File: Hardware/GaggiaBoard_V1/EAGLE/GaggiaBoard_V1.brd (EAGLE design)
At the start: 80 x 100 mm, 64 parts, among them IC1 LD117ADT33TR, J2 Vertical Qwiic Connector, J3 Vertical Qwiic Connector, J4 1X2-3.5MM, J5 1X2-3.5MM, K1 RELAY-SPDT-JZC-11F, K2 RELAY-SPDT-JZC-11F, K3 RELAY-SPDT-JZC-11F, Q1 600mA/40V, Q2 600mA/40V, Q3 600mA/40V, Q4 600mA/40V, Q5 600mA/40V, Q6 600mA/40V, U1 BLACKPILL, U2 MAX31855K, U3 MAX31855K, U4 MOC3021MDIL06O

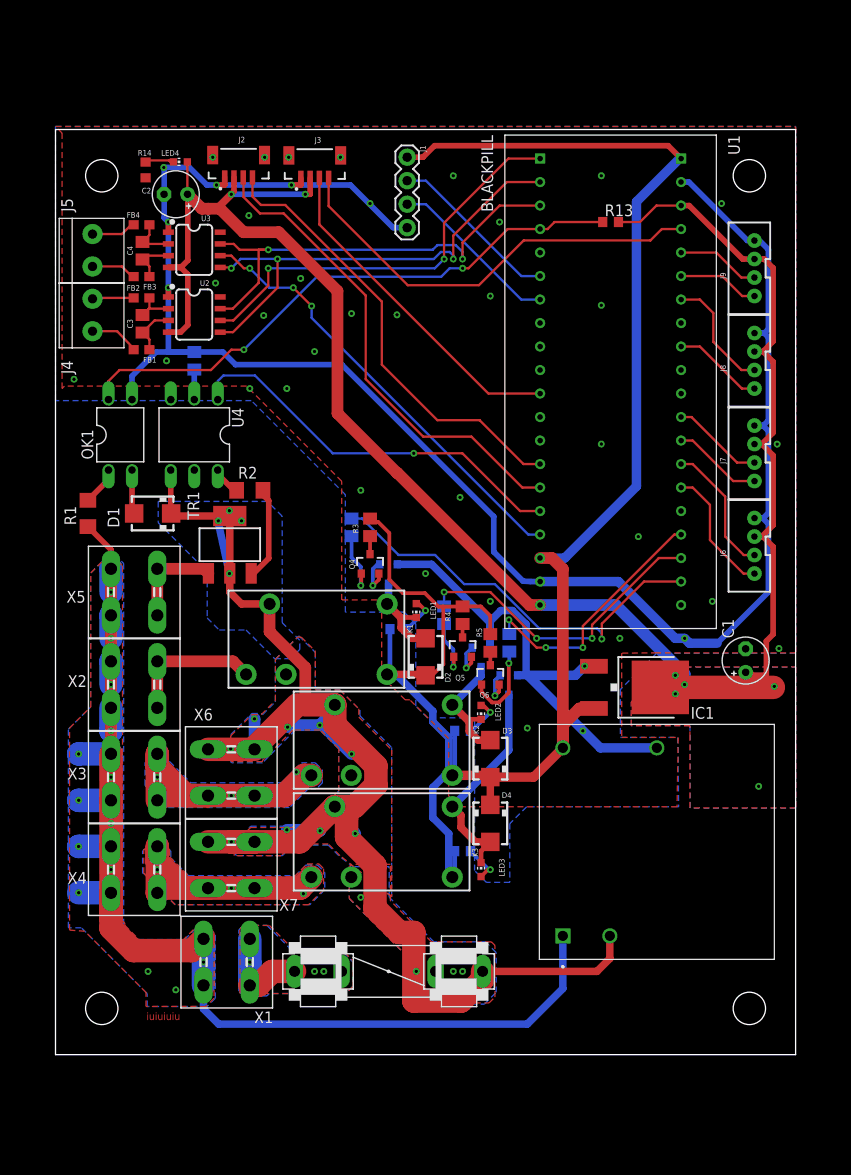
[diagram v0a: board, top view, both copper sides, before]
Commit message: Fiducials added
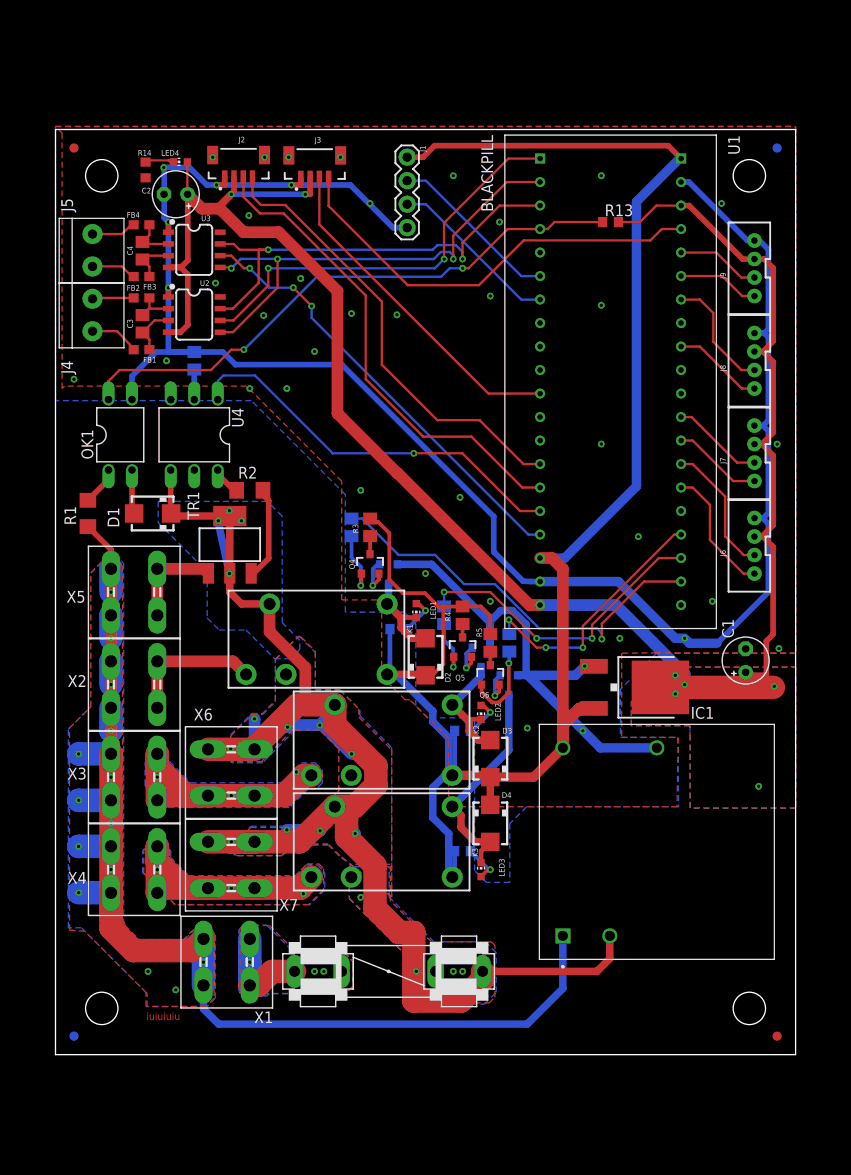
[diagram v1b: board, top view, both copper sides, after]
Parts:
- added MARK1, MARK2, MARK3, MARK4: FIDUCIAL, adafruit:FIDUCIAL_1MM
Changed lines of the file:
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@@
 <setting verticaltext="up"/>
 </settings>
-<grid distance="50" unitdist="mil" unit="mil" style="lines" multiple="1" display="no" altdistance="5" altunitdist="mil" altunit="mil"/>
+<grid distance="1" unitdist="mm" unit="mm" style="lines" multiple="1" display="no" altdistance="0.1" altunitdist="mm" altunit="mm"/>
 <layers>
 <layer number="1" name="Top" color="4" fill="1" visible="yes" active="yes"/>
@@
 <attribute name="VALUE" x="11.643" y="94.992" size="1.27" layer="27" rot="R90"/>
 </element>
+<element name="MARK2" library="adafruit" library_urn="urn:adsk.eagle:library:420" package="FIDUCIAL_1MM" package3d_urn="urn:adsk.eagle:package:6240632/1" value="FIDUCIAL" x="2" y="2" smashed="yes" rot="MR0"/>
+<element name="MARK4" library="adafruit" library_urn="urn:adsk.eagle:library:420" package="FIDUCIAL_1MM" package3d_urn="urn:adsk.eagle:package:6240632/1" value="FIDUCIAL" x="78" y="98" smashed="yes" rot="MR0"/>
+<element name="MARK3" library="adafruit" library_urn="urn:adsk.eagle:library:420" package="FIDUCIAL_1MM" package3d_urn="urn:adsk.eagle:package:6240632/1" value="FIDUCIAL" x="78" y="2" smashed="yes"/>
+<element name="MARK1" library="adafruit" library_urn="urn:adsk.eagle:library:420" package="FIDUCIAL_1MM" package3d_urn="urn:adsk.eagle:package:6240632/1" value="FIDUCIAL" x="2" y="98" smashed="yes"/>
 </elements>
 <signals>

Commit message: UART level shifter
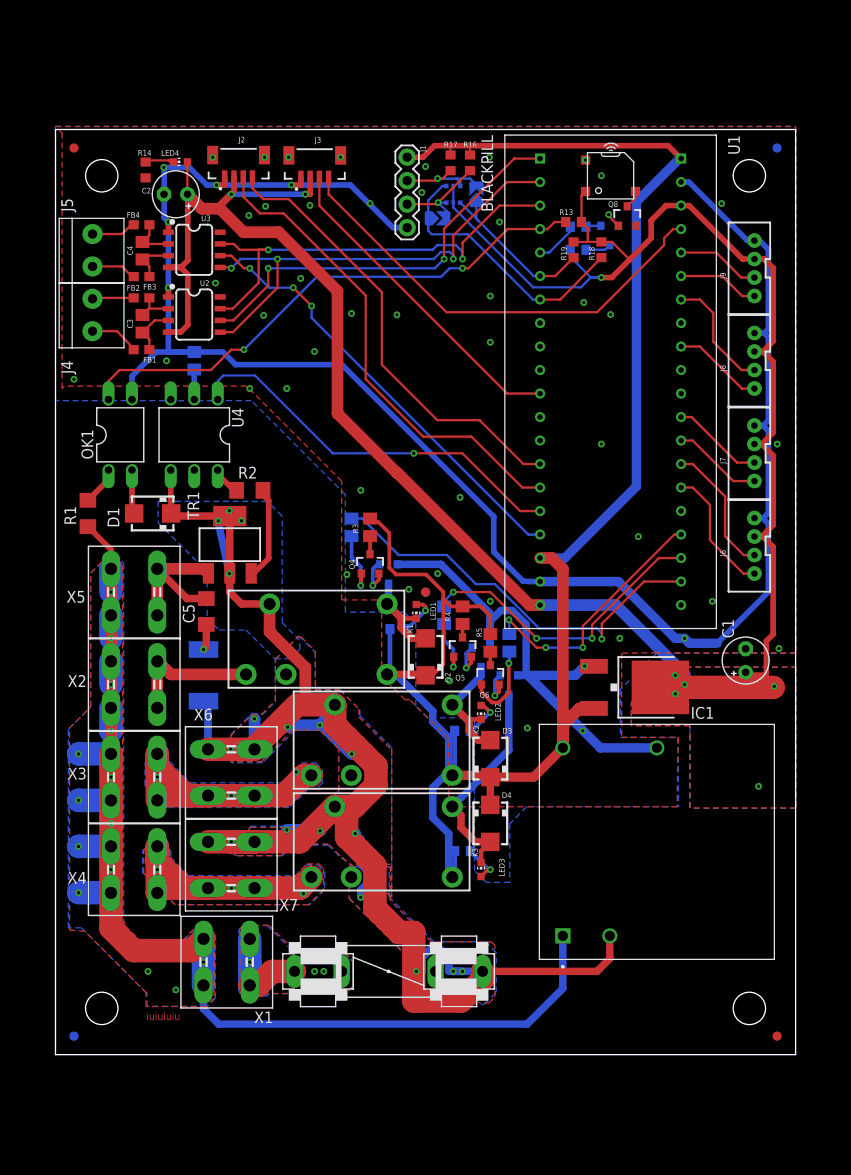
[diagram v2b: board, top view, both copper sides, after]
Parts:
- added C5: 10nF, rcl:C1206
- added MARK5, MARK6: FIDUCIAL, adafruit:FIDUCIAL_1MM
- added Q7: (no value), microbuilder:SOT363
- added Q8, Q9: 600mA/40V, SparkFun-DiscreteSemi:SOT23-3
- added R15: 220, rcl:R2512
- added R16, R17, R18, R19, R20, R21: 10K, rcl:R0603
- added SJ1, SJ2: (no value), microbuilder:SOLDERJUMPER_ARROW_NOPASTE
- added SPK1: SMT-0540-S-R, adafruit:SMT-0540-S-R
- moved R13 4.00 mm to (56.0, 90.0)
- moved LED1 0.10 mm to (39.0, 47.9)
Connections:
- new net N$30: Q8.3, SPK1.-
- new net N$32: C5.1, R15.2
- new net N$33: Q8.1, Q9.2
- new net N$34: Q9.1, R20.2
- new net N$35: Q9.3, R21.1
- new net PA8: R20.1, U1.P1$5
- new net UART1_5V_RX: J1.3, Q7.3, R16.1, SJ2.2
- new net UART1_5V_TX: J1.2, Q7.6, R17.1, SJ1.2
- net 3V3: now also Q7.2, Q7.5, R18.2, R19.2, R21.2, SPK1.+
- net 5V: now also R16.2, R17.2
- net AC_P: now also R15.1
- net GND: now also Q8.2
- net PUMP_P: now also C5.2
- net UART1_RX: now also Q7.4, R18.1, SJ2.1; no longer J1.3
- net UART1_TX: now also Q7.1, R19.1, SJ1.1; no longer J1.2
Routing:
- net 3V3: track 215.8 -> 257.8 mm, vias 7 -> 8
- net AC_P: track 179.6 -> 204.6 mm
- net UART1_5V_RX: track 0.00 -> 11.3 mm, vias 0 -> 1
- net UART1_RX: track 18.6 -> 29.6 mm
- net UART1_5V_TX: track 0.00 -> 10.6 mm, vias 0 -> 1
- net PUMP_P: track 10.8 -> 17.4 mm
- net AC_N: track 148.0 -> 141.9 mm
- net PA8: track 0.00 -> 4.73 mm
- net PB15: track 62.5 -> 58.5 mm
- net N$33: track 0.00 -> 3.27 mm, vias 0 -> 1
- net N$32: track 0.00 -> 2.82 mm, vias 0 -> 1
- net N$35: track 0.00 -> 2.76 mm
- net 5V: track 202.8 -> 205.4 mm
- net I2C2_SCL: track 47.2 -> 49.3 mm
- net N$30: track 0.00 -> 1.97 mm
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
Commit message: GaggiaBoard BOM update
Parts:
- Q7: value (none) -> 2N7002D
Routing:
- net GND: track 259.1 -> 260.3 mm
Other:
- outline, holes or cut-outs redrawn

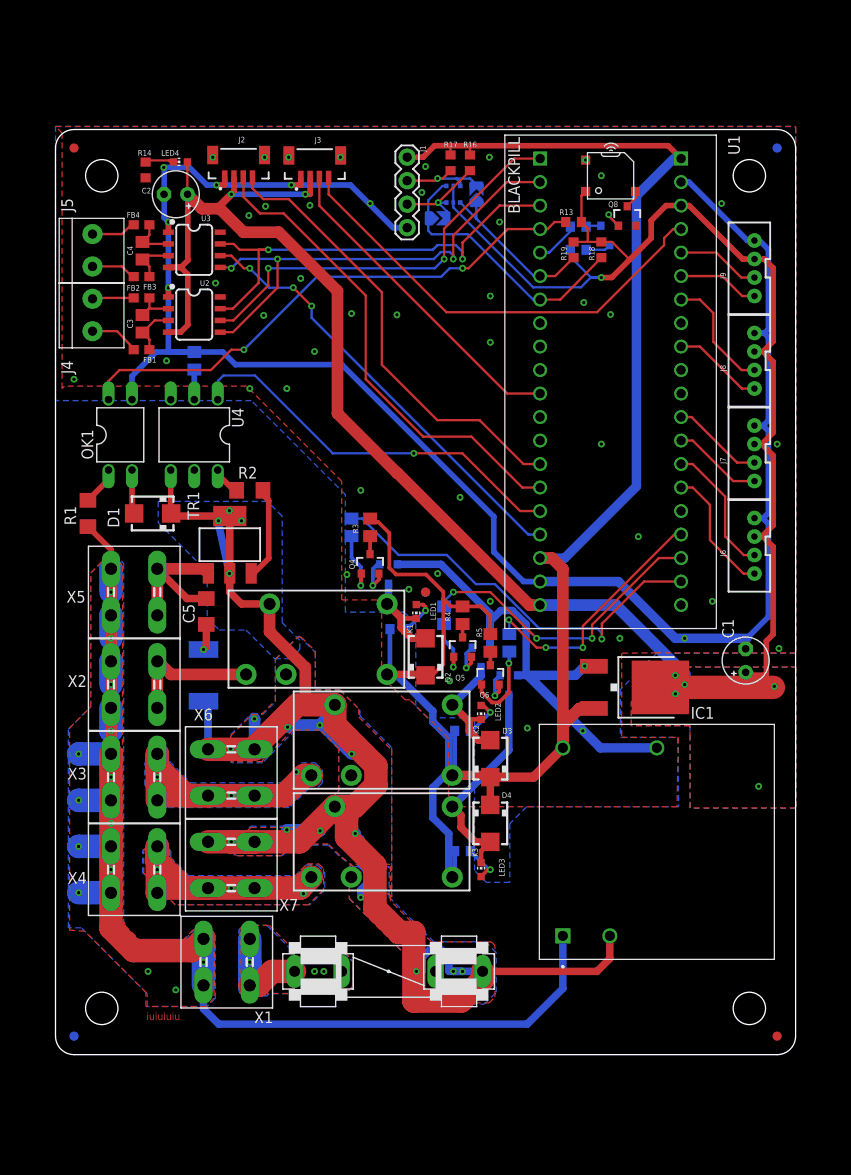
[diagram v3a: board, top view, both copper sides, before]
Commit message: Warning symbols added
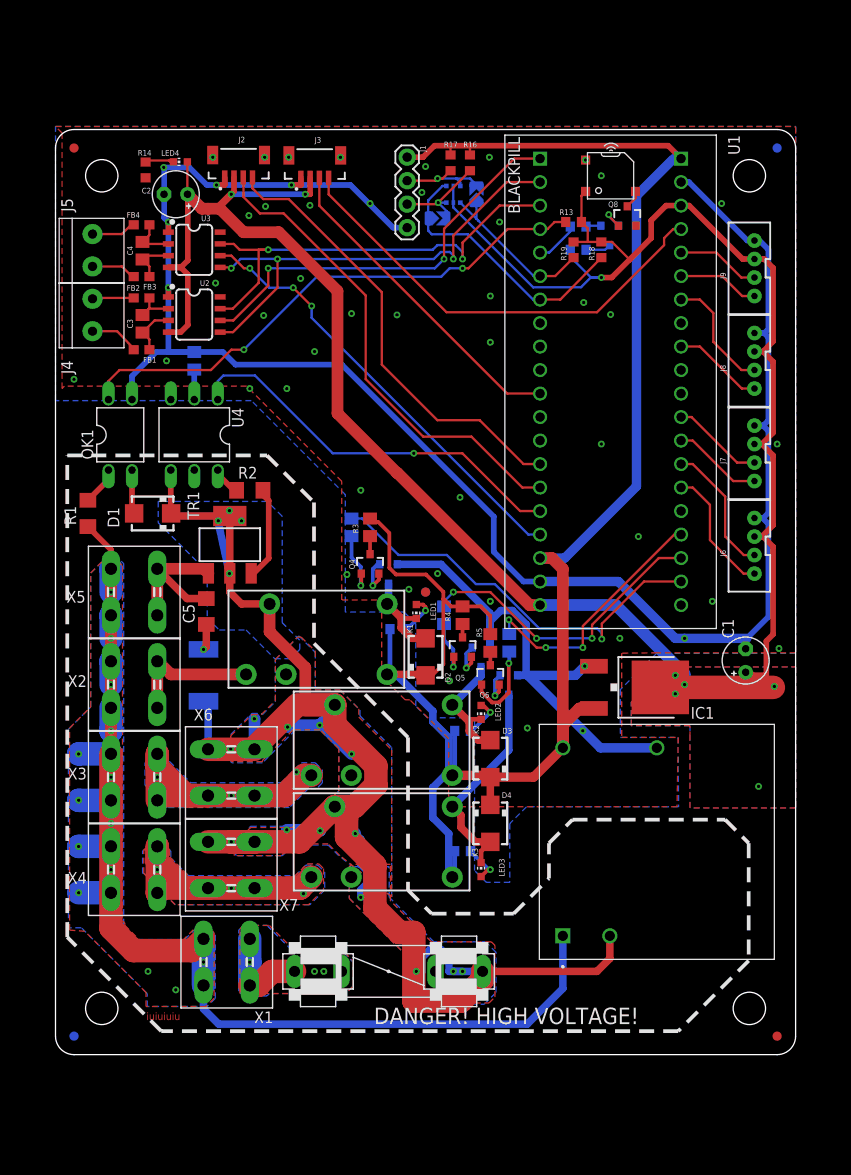
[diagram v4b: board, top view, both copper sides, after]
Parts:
- added U$1: (no value), discrete:HV_LOGO_3
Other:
- board text added: "DANGER! HIGH VOLTAGE!"
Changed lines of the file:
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@@
 <setting verticaltext="up"/>
 </settings>
-<grid distance="1" unitdist="mm" unit="mm" style="lines" multiple="1" display="no" altdistance="0.1" altunitdist="mm" altunit="mm"/>
+<grid distance="50" unitdist="mil" unit="mil" style="lines" multiple="1" display="no" altdistance="5" altunitdist="mil" altunit="mil"/>
 <layers>
 <layer number="1" name="Top" color="4" fill="1" visible="yes" active="yes"/>
@@
 <wire x1="80" y1="2" x2="78" y2="0" width="0" layer="20" curve="-90"/>
 <wire x1="0" y1="2" x2="2" y2="0" width="0" layer="20" curve="90"/>
+<wire x1="1.27" y1="64.77" x2="22.86" y2="64.77" width="0.4064" layer="21" style="shortdash"/>
+<wire x1="22.86" y1="64.77" x2="27.94" y2="59.69" width="0.4064" layer="21" style="shortdash"/>
+<wire x1="27.94" y1="59.69" x2="27.94" y2="44.45" width="0.4064" layer="21" style="shortdash"/>
+<wire x1="27.94" y1="44.45" x2="38.1" y2="34.29" width="0.4064" layer="21" style="shortdash"/>
+<wire x1="38.1" y1="34.29" x2="38.1" y2="17.78" width="0.4064" layer="21" style="shortdash"/>
+<wire x1="38.1" y1="17.78" x2="40.64" y2="15.24" width="0.4064" layer="21" style="shortdash"/>
+<wire x1="40.64" y1="15.24" x2="49.53" y2="15.24" width="0.4064" layer="21" style="shortdash"/>
+<wire x1="49.53" y1="15.24" x2="53.34" y2="19.05" width="0.4064" layer="21" style="shortdash"/>
+<wire x1="53.34" y1="19.05" x2="53.34" y2="22.86" width="0.4064" layer="21" style="shortdash"/>
+<wire x1="53.34" y1="22.86" x2="55.88" y2="25.4" width="0.4064" layer="21" style="shortdash"/>
+<wire x1="55.88" y1="25.4" x2="72.39" y2="25.4" width="0.4064" layer="21" style="shortdash"/>
+<wire x1="72.39" y1="25.4" x2="74.93" y2="22.86" width="0.4064" layer="21" style="shortdash"/>
+<wire x1="74.93" y1="22.86" x2="74.93" y2="10.16" width="0.4064" layer="21" style="shortdash"/>
+<wire x1="74.93" y1="10.16" x2="67.31" y2="2.54" width="0.4064" layer="21" style="shortdash"/>
+<wire x1="67.31" y1="2.54" x2="11.43" y2="2.54" width="0.4064" layer="21" style="shortdash"/>
+<wire x1="11.43" y1="2.54" x2="1.27" y2="12.7" width="0.4064" layer="21" style="shortdash"/>
+<wire x1="1.27" y1="12.7" x2="1.27" y2="64.77" width="0.4064" layer="21" style="shortdash"/>
+<text x="62.357" y="3.302" size="1.778" layer="22" rot="MR0">DANGER! HIGH VOLTAGE!</text>
+<wire x1="1.27" y1="64.77" x2="22.86" y2="64.77" width="0.4064" layer="22" style="shortdash"/>
+<wire x1="22.86" y1="64.77" x2="27.94" y2="59.69" width="0.4064" layer="22" style="shortdash"/>
+<wire x1="27.94" y1="59.69" x2="27.94" y2="44.45" width="0.4064" layer="22" style="shortdash"/>
+<wire x1="27.94" y1="44.45" x2="38.1" y2="34.29" width="0.4064" layer="22" style="shortdash"/>
+<wire x1="38.1" y1="34.29" x2="38.1" y2="17.78" width="0.4064" layer="22" style="shortdash"/>
+<wire x1="38.1" y1="17.78" x2="40.64" y2="15.24" width="0.4064" layer="22" style="shortdash"/>
+<wire x1="40.64" y1="15.24" x2="49.53" y2="15.24" width="0.4064" layer="22" style="shortdash"/>
+<wire x1="49.53" y1="15.24" x2="53.34" y2="19.05" width="0.4064" layer="22" style="shortdash"/>
+<wire x1="53.34" y1="19.05" x2="53.34" y2="22.86" width="0.4064" layer="22" style="shortdash"/>
+<wire x1="53.34" y1="22.86" x2="55.88" y2="25.4" width="0.4064" layer="22" style="shortdash"/>
+<wire x1="55.88" y1="25.4" x2="72.39" y2="25.4" width="0.4064" layer="22" style="shortdash"/>
+<wire x1="72.39" y1="25.4" x2="74.93" y2="22.86" width="0.4064" layer="22" style="shortdash"/>
+<wire x1="74.93" y1="22.86" x2="74.93" y2="10.16" width="0.4064" layer="22" style="shortdash"/>
+<wire x1="74.93" y1="10.16" x2="67.31" y2="2.54" width="0.4064" layer="22" style="shortdash"/>
+<wire x1="67.31" y1="2.54" x2="11.43" y2="2.54" width="0.4064" layer="22" style="shortdash"/>
+<wire x1="11.43" y1="2.54" x2="1.27" y2="12.7" width="0.4064" layer="22" style="shortdash"/>
+<wire x1="1.27" y1="12.7" x2="1.27" y2="64.77" width="0.4064" layer="22" style="shortdash"/>
+<text x="34.417" y="3.302" size="1.778" layer="21">DANGER! HIGH VOLTAGE!</text>
 </plain>
 <attributes>
@@
 <element name="MARK5" library="adafruit" library_urn="urn:adsk.eagle:library:420" package="FIDUCIAL_1MM" package3d_urn="urn:adsk.eagle:package:6240632/1" value="FIDUCIAL" x="40" y="50" smashed="yes"/>
 <element name="MARK6" library="adafruit" library_urn="urn:adsk.eagle:library:420" package="FIDUCIAL_1MM" package3d_urn="urn:adsk.eagle:package:6240632/1" value="FIDUCIAL" x="40" y="50" smashed="yes" rot="MR0"/>
+<element name="U$1" library="discrete" package="HV_LOGO_3" value="" x="72" y="8" smashed="yes" rot="MR0"/>
 </elements>
 <signals>
@@
 packages will not be understood (or retained) with this version.
 </note>
+<note version="8.5" severity="warning">
+Since Version 8.5, EAGLE supports locking for holes, vias, wires and polygons.
+The locking property on all objects of these types will not be understood in this version.
+</note>
 </compatibility>
